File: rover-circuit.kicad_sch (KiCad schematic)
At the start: 9 parts, among them J4 Conn_01x04_Socket

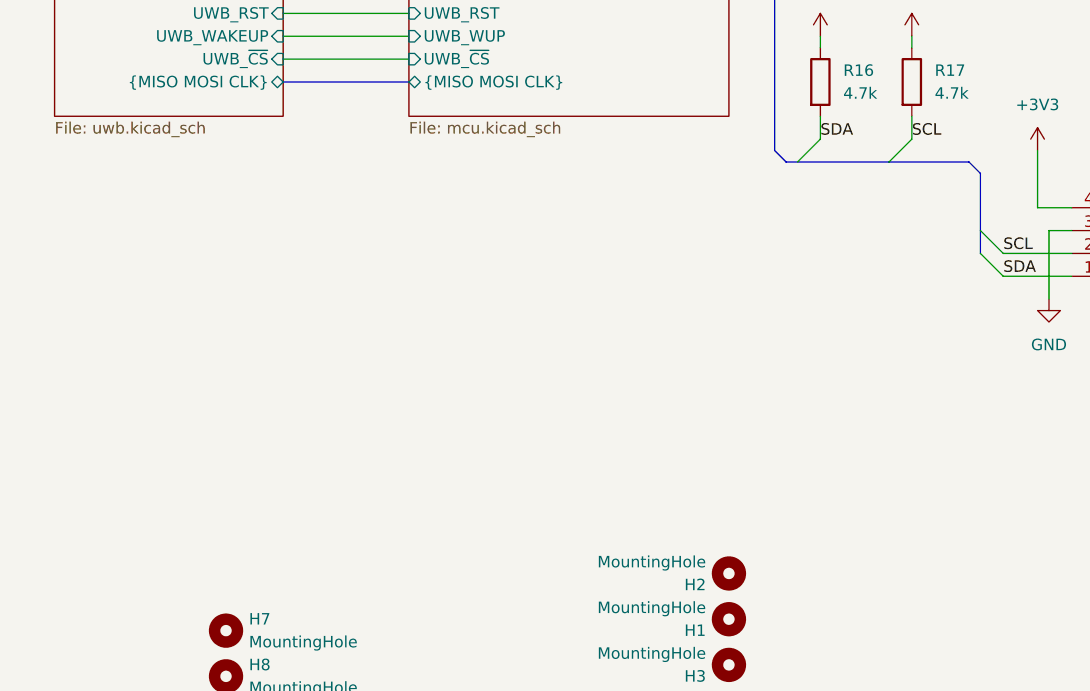
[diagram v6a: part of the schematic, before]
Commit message: annotate with LCSC components
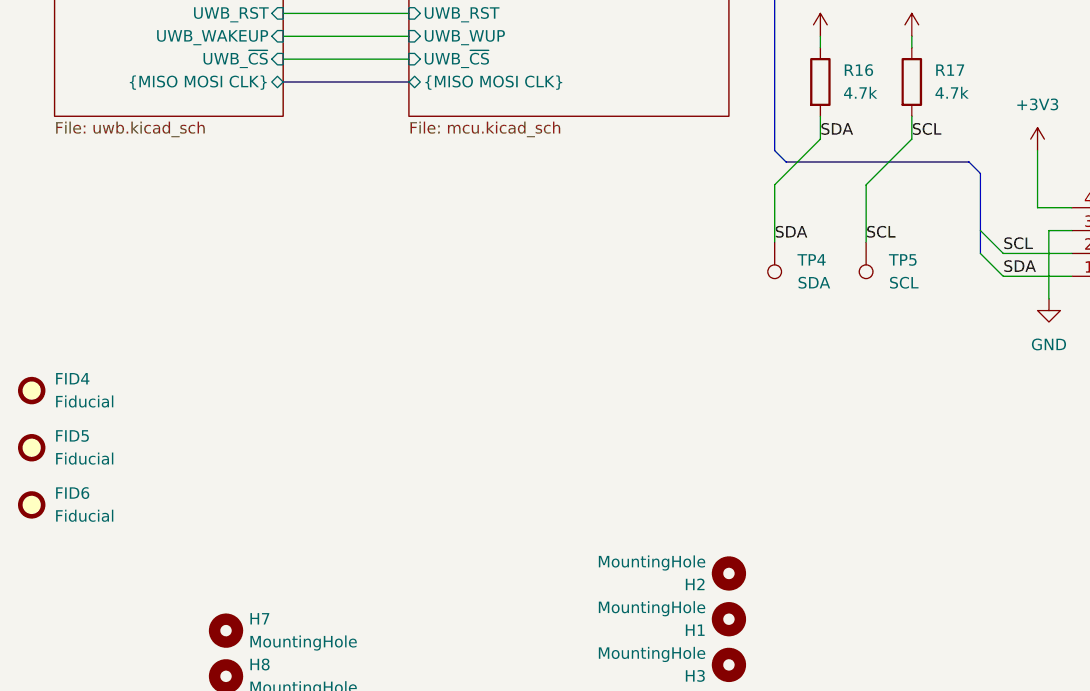
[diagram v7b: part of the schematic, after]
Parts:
- added FID4, FID5, FID6: Fiducial, Fiducial:Fiducial_0.5mm_Mask1mm, symbol Mechanical:Fiducial
- added TP4: SDA, TestPoint:TestPoint_Pad_D1.0mm, symbol Connector:TestPoint
- added TP5: SCL, TestPoint:TestPoint_Pad_D1.0mm, symbol Connector:TestPoint
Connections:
- net SCL: now also TP5.1
- net SDA: now also TP4.1

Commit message: finalized component selection
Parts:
- H7, H8: value MountingHole -> Raspberry
- J4: value Conn_01x04_Socket -> Proximity
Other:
- moved on the sheet: FID4, FID5, FID6, H7, H8
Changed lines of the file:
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@@
 			)
 		)
-		(property "Value" "Conn_01x04_Socket"
+		(property "Value" "Proximity"
 			(at 201.93 137.1601 0)
 			(show_name no)
@@
 	(symbol
 		(lib_id "Mechanical:Fiducial")
-		(at 80.01 167.64 0)
+		(at 91.44 187.96 0)
 		(unit 1)
 		(body_style 1)
@@
 		(fields_autoplaced yes)
 		(property "Reference" "FID6"
-			(at 82.55 166.3699 0)
+			(at 93.98 186.6899 0)
 			(show_name no)
 			(do_not_autoplace no)
@@
 		)
 		(property "Value" "Fiducial"
-			(at 82.55 168.9099 0)
+			(at 93.98 189.2299 0)
 			(show_name no)
 			(do_not_autoplace no)
@@
 		)
 		(property "Footprint" "Fiducial:Fiducial_0.5mm_Mask1mm"
-			(at 80.01 167.64 0)
+			(at 91.44 187.96 0)
 			(hide yes)
 			(show_name no)
@@
 		)
 		(property "Datasheet" ""
-			(at 80.01 167.64 0)
+			(at 91.44 187.96 0)
 			(hide yes)
 			(show_name no)
@@
 		)
 		(property "Description" "Fiducial Marker"
-			(at 80.01 167.64 0)
+			(at 91.44 187.96 0)
 			(hide yes)
 			(show_name no)
@@
 	(symbol
 		(lib_id "Mechanical:MountingHole")
-		(at 101.6 186.69 0)
+		(at 115.57 186.69 0)
 		(unit 1)
 		(body_style 1)
@@
 		(fields_autoplaced yes)
 		(property "Reference" "H8"
-			(at 104.14 185.4199 0)
-			(show_name no)
-			(do_not_autoplace no)
-			(effects
-				(font
-					(size 1.27 1.27)
-				)
-				(justify left)
-			)
-		)
-		(property "Value" "MountingHole"
-			(at 104.14 187.9599 0)
+			(at 118.11 185.4199 0)
+			(show_name no)
+			(do_not_autoplace no)
+			(effects
+				(font
+					(size 1.27 1.27)
+				)
+				(justify left)
+			)
+		)
+		(property "Value" "Raspberry"
+			(at 118.11 187.9599 0)
 			(show_name no)
 			(do_not_autoplace no)
@@
 		)
 		(property "Footprint" "MountingHole:MountingHole_2.5mm"
-			(at 101.6 186.69 0)
+			(at 115.57 186.69 0)
 			(hide yes)
 			(show_name no)
@@
 		)
 		(property "Datasheet" ""
-			(at 101.6 186.69 0)
+			(at 115.57 186.69 0)
 			(hide yes)
 			(show_name no)
@@
 		)
 		(property "Description" "Mounting Hole without connection"
-			(at 101.6 186.69 0)
+			(at 115.57 186.69 0)
 			(hide yes)
 			(show_name no)
@@
 	(symbol
 		(lib_id "Mechanical:Fiducial")
-		(at 80.01 161.29 0)
+		(at 91.44 181.61 0)
 		(unit 1)
 		(body_style 1)
@@
 		(fields_autoplaced yes)
 		(property "Reference" "FID5"
-			(at 82.55 160.0199 0)
+			(at 93.98 180.3399 0)
 			(show_name no)
 			(do_not_autoplace no)
@@
 		)
 		(property "Value" "Fiducial"
-			(at 82.55 162.5599 0)
+			(at 93.98 182.8799 0)
 			(show_name no)
 			(do_not_autoplace no)
@@
 		)
 		(property "Footprint" "Fiducial:Fiducial_0.5mm_Mask1mm"
-			(at 80.01 161.29 0)
+			(at 91.44 181.61 0)
 			(hide yes)
 			(show_name no)
@@
 		)
 		(property "Datasheet" ""
-			(at 80.01 161.29 0)
+			(at 91.44 181.61 0)
 			(hide yes)
 			(show_name no)
@@
 		)
 		(property "Description" "Fiducial Marker"
-			(at 80.01 161.29 0)
+			(at 91.44 181.61 0)
 			(hide yes)
 			(show_name no)
@@
 	(symbol
 		(lib_id "Mechanical:MountingHole")
-		(at 101.6 181.61 0)
+		(at 115.57 181.61 0)
 		(unit 1)
 		(body_style 1)
@@
 		(fields_autoplaced yes)
 		(property "Reference" "H7"
-			(at 104.14 180.3399 0)
-			(show_name no)
-			(do_not_autoplace no)
-			(effects
-				(font
-					(size 1.27 1.27)
-				)
-				(justify left)
-			)
-		)
-		(property "Value" "MountingHole"
-			(at 104.14 182.8799 0)
+			(at 118.11 180.3399 0)
+			(show_name no)
+			(do_not_autoplace no)
+			(effects
+				(font
+					(size 1.27 1.27)
+				)
+				(justify left)
+			)
+		)
+		(property "Value" "Raspberry"
+			(at 118.11 182.8799 0)
 			(show_name no)
 			(do_not_autoplace no)
@@
 		)
 		(property "Footprint" "MountingHole:MountingHole_2.5mm"
-			(at 101.6 181.61 0)
+			(at 115.57 181.61 0)
 			(hide yes)
 			(show_name no)
@@
 		)
 		(property "Datasheet" ""
-			(at 101.6 181.61 0)
+			(at 115.57 181.61 0)
 			(hide yes)
 			(show_name no)
@@
 		)
 		(property "Description" "Mounting Hole without connection"
-			(at 101.6 181.61 0)
+			(at 115.57 181.61 0)
 			(hide yes)
 			(show_name no)
@@
 	(symbol
 		(lib_id "Mechanical:Fiducial")
-		(at 80.01 154.94 0)
+		(at 91.44 175.26 0)
 		(unit 1)
 		(body_style 1)
@@
 		(fields_autoplaced yes)
 		(property "Reference" "FID4"
-			(at 82.55 153.6699 0)
+			(at 93.98 173.9899 0)
 			(show_name no)
 			(do_not_autoplace no)
@@
 		)
 		(property "Value" "Fiducial"
-			(at 82.55 156.2099 0)
+			(at 93.98 176.5299 0)
 			(show_name no)
 			(do_not_autoplace no)
@@
 		)
 		(property "Footprint" "Fiducial:Fiducial_0.5mm_Mask1mm"
-			(at 80.01 154.94 0)
+			(at 91.44 175.26 0)
 			(hide yes)
 			(show_name no)
@@
 		)
 		(property "Datasheet" ""
-			(at 80.01 154.94 0)
+			(at 91.44 175.26 0)
 			(hide yes)
 			(show_name no)
@@
 		)
 		(property "Description" "Fiducial Marker"
-			(at 80.01 154.94 0)
-			(hide yes)
-			(show_name no)
+			(at 91.44 175.26 0)
+			(hide yes)
+			(show_name no)
